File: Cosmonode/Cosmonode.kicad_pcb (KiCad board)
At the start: 2 copper layers, 47 x 34.3 mm, 36 parts, among them J1 CONN_01X08, J10 WEEE_Logo, J11 Aloes_Logo, J12 Aloes_mini_Logo, J2 CONN_01X08, J3 CONN_01X09, J4 OSHW, J5 CONN_01X02, J6 GS3, J7 Kicad_Logo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

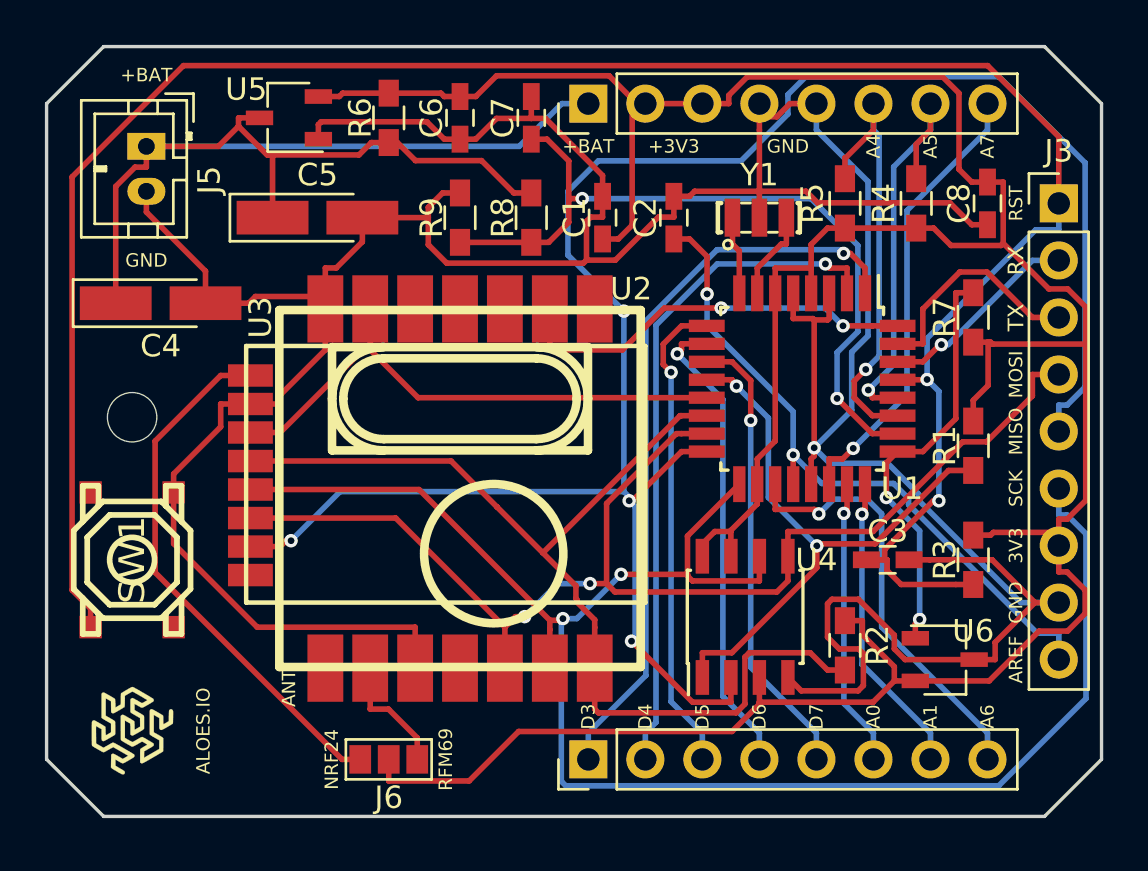
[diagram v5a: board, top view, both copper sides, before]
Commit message: update to v0.5 ( base, ext05, ext07, ext08 )
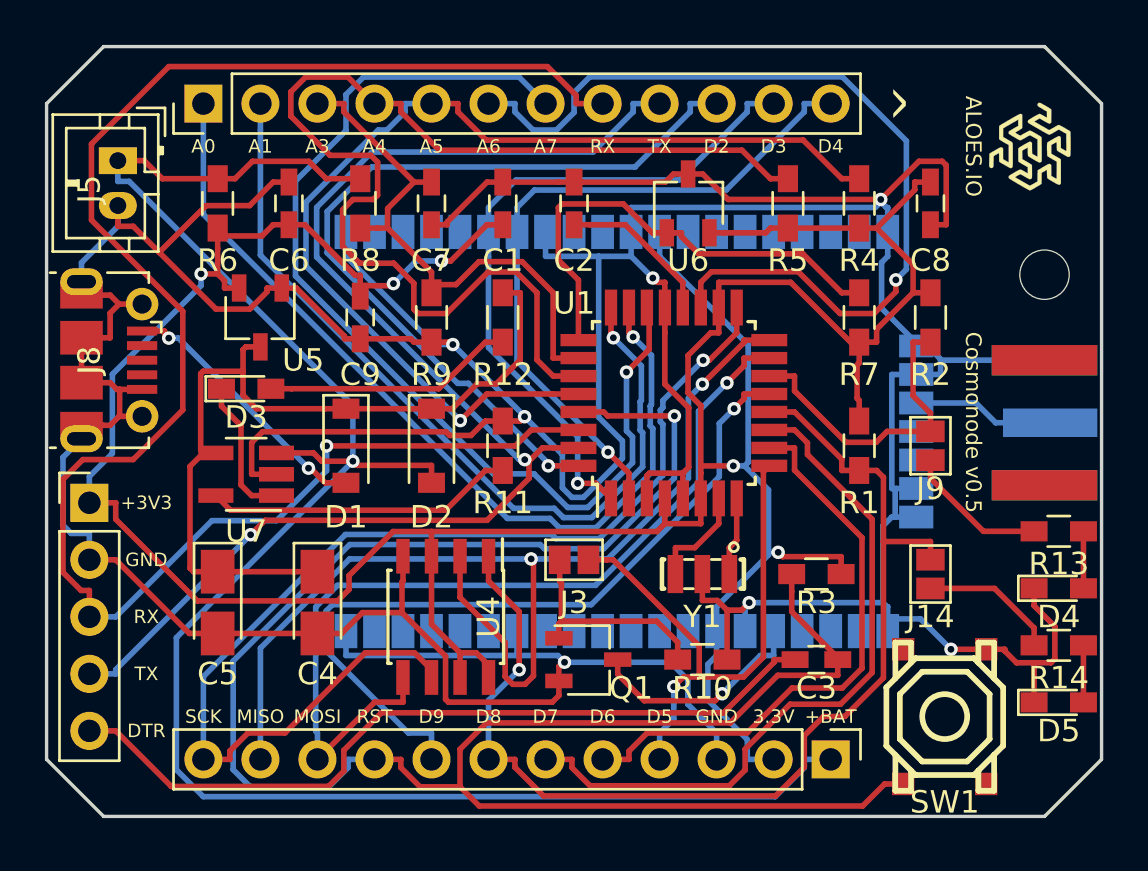
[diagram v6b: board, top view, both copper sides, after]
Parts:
- removed J6: GS3, Connectors:GS3
- removed J7: Kicad_Logo, Symbols:KiCad-Logo2_6mm_SilkScreen
- removed U2: RFM69CW, w_rf_modules:RFM12B_SMD
- added C9: 100nF, Capacitors_SMD:C_0603_HandSoldering, F.Cu at (160.0, 89.5)
- added D1: MBR0520, Diodes_SMD:D_SOD-123, F.Cu at (159.4, 95.2)
- added D2: MBR0520, Diodes_SMD:D_SOD-123, F.Cu at (163.2, 95.2)
- added D3: LED, LEDs:LED_0603_HandSoldering, F.Cu at (154.9, 92.7)
- added D4: LED, LEDs:LED_0603_HandSoldering, F.Cu at (191.1, 101.6)
- added D5: LED, LEDs:LED_0603_HandSoldering, F.Cu at (191.1, 106.7)
- added J13: CONN_01X05, Pin_Headers:Pin_Header_Straight_1x05_Pitch2.54mm, F.Cu at (148.0, 97.8)
- added J14: GS2, Connectors:GS2, F.Cu at (185.4, 101.0)
- added J8: USB_OTG, Connectors_USB:USB_Micro-B_Molex-105017-0001, F.Cu at (148.0, 91.4)
- added J9: GS2, Connectors:GS2, F.Cu at (185.4, 95.2)
- added P1: COAX, sma:EDGE_SMA_5, B.Cu at (190.5, 91.4)
- added Q1: BSS123, TO_SOT_Packages_SMD:TSOT-23, F.Cu at (170.2, 104.8)
- added R10: 10k, Resistors_SMD:R_0603_HandSoldering, F.Cu at (175.3, 104.8)
- added R11: R, Resistors_SMD:R_0603_HandSoldering, F.Cu at (166.4, 95.2)
- added R12: 1k, Resistors_SMD:R_0603_HandSoldering, F.Cu at (166.4, 89.5)
- added R13: 1k, Resistors_SMD:R_0603_HandSoldering, F.Cu at (191.1, 99.1)
- added R14: 1k, Resistors_SMD:R_0603_HandSoldering, F.Cu at (191.1, 104.1)
- added U7: MCP73811T-420I/OT, TO_SOT_Packages_SMD:SOT-23-5_HandSoldering, F.Cu at (154.9, 96.5)
- C4, C5: footprint Capacitors_Tantalum_SMD:CP_Tantalum_Case-A_EIA-3216-18_Hand -> Capacitors_Tantalum_SMD:CP_Tantalum_Case-A_EIA-3216-18_Reflow
- J1, J2: value CONN_01X08 -> CONN_01X12; footprint Pin_Headers:Pin_Header_Straight_1x08_Pitch2.54mm -> Pin_Headers:Pin_Header_Straight_1x12_Pitch2.54mm
- J3: value CONN_01X09 -> GS2; footprint Pin_Headers:Pin_Header_Straight_1x09_Pitch2.54mm -> Connectors:GS2
- U3: value NRF24L01_Breakout -> RN2483; footprint mysensors_radios:NRF24L01-SMD -> RN2483:RN2483; moved to B.Cu
- moved J12 47.7 mm to (189.9, 81.9), turned to 270 degrees
- moved MK1 41.1 mm to (190.5, 87.6)
- moved SW1 36.9 mm to (186.1, 107.3)
- moved J11 35.8 mm to (187.3, 82.5), turned to 90 degrees
- moved J1 33.9 mm to (153.0, 80.0)
- moved J2 31.1 mm to (181.0, 109.2), turned to 270 degrees
- moved J3 26.8 mm to (169.5, 100.3), turned to 90 degrees
- moved U6 23.3 mm to (174.6, 84.5), turned to 90 degrees
- moved C5 17.7 mm to (153.7, 102.2), turned to 270 degrees
- moved Y1 16.1 mm to (175.3, 101.0), turned to 180 degrees
- moved R2 15.1 mm to (185.4, 89.5)
- moved C4 15.1 mm to (158.1, 102.2), turned to 270 degrees
- moved U4 13.3 mm to (163.8, 102.9), turned to 270 degrees
- moved J4 12.8 mm to (188.6, 102.2), turned to 90 degrees
- moved U3 9.03 mm to (158.1, 103.5), turned to 90 degrees
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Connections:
- net /A2 renamed A2
- C3 pad 1: /RST -> RST
- C3 pad 2: GND -> DTR
- C4 pad 1: /BAT+ -> Net-(C4-Pad1)
- C5 pad 1: /BAT+ -> Net-(C4-Pad1)
- C7 pad 2: /A3 -> A3
- J1 pad 1: /D3 -> A0
- J1 pad 2: /D4 -> A1
- J1 pad 3: /D5 -> A3
- J1 pad 4: /D6 -> A4
- J1 pad 5: /D7 -> A5
- J1 pad 6: /A0 -> A6
- J1 pad 7: /A1 -> A7
- J1 pad 8: /A6 -> RX
- J2 pad 1: /BAT+ -> +BATT
- J2 pad 3: +3V3 -> GND
- J2 pad 4: GND -> D5
- J2 pad 5: GND -> D6
- J2 pad 6: /A4 -> D7
- J2 pad 7: /A5 -> D8
- J2 pad 8: /A7 -> D9
- J3 pad 1: /RST -> Net-(J3-Pad1)
- J3 pad 2: /RX -> D5
- J5 pad 1: /BAT+ -> +BATT
- R1 pad 2: /D8 -> D8
- R2 pad 2: /D10 -> D10
- R3 pad 2: /RST -> RST
- R4 pad 2: /A5 -> A5
- R5 pad 2: /A4 -> A4
- R6 pad 2: /BAT+ -> +BATT
- R8 pad 1: /BAT+ -> +BATT
- R8 pad 2: /A3 -> A3
- R9 pad 1: /A3 -> A3
- SW1 pad 2: /RST -> RST
- U1 pad 1: /D3 -> D3
- U1 pad 10: /D6 -> D6
- U1 pad 11: /D7 -> D7
- U1 pad 12: /D8 -> D8
- U1 pad 13: /D9 -> D9
- U1 pad 14: /D10 -> D10
- U1 pad 15: /MOSI -> MOSI
- U1 pad 16: /MISO -> MISO
- U1 pad 17: /SCK -> SCK
- U1 pad 19: /A6 -> A6
- U1 pad 2: /D4 -> D4
- U1 pad 22: /A7 -> A7
- U1 pad 23: /A0 -> A0
- U1 pad 24: /A1 -> A1
- U1 pad 26: /A3 -> A3
- U1 pad 27: /A4 -> A4
- U1 pad 28: /A5 -> A5
- U1 pad 29: /RST -> RST
- U1 pad 30: /RX -> RX
- U1 pad 31: /TX -> TX
- U1 pad 32: /D2 -> D2
- U1 pad 9: /D5 -> D5
- U3 pad 2: /VCC_NRF24 -> Net-(U3-Pad2)
- U3 pad 3: /D9 -> Net-(U3-Pad3)
- U3 pad 4: /D10 -> Net-(U3-Pad4)
- U3 pad 5: /SCK -> Net-(U3-Pad5)
- U3 pad 6: /MOSI -> D3
- U3 pad 7: /MISO -> D4
- U3 pad 8: Net-(U3-Pad8) -> GND
- U4 pad 1: /D8 -> D8
- U4 pad 2: /MISO -> MISO
- U4 pad 5: /MOSI -> MOSI
- U4 pad 6: /SCK -> SCK
- U5 pad 3: /BAT+ -> Net-(C4-Pad1)
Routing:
- net /RST: track 97.8 -> 0.00 mm, vias 2 -> 0
- net RST: track 0.00 -> 92.7 mm, vias 0 -> 1
- net /MISO: track 91.3 -> 0.00 mm, vias 4 -> 0
- net GND: track 178.6 -> 268.2 mm, vias 1 -> 7
- net +BATT: track 0.00 -> 85.2 mm, vias 0 -> 1
- net RX: track 0.00 -> 77.9 mm, vias 0 -> 1
- net /SCK: track 76.7 -> 0.00 mm, vias 2 -> 0
- net TX: track 0.00 -> 59.4 mm, vias 0 -> 2
- net /MOSI: track 56.0 -> 0.00 mm, vias 2 -> 0
- net A4: track 0.00 -> 52.1 mm
- net /BAT+: track 51.6 -> 0.00 mm
- net SCK: track 0.00 -> 50.1 mm, vias 0 -> 1
- net D8: track 0.00 -> 50.1 mm, vias 0 -> 1
- net MISO: track 0.00 -> 48.5 mm, vias 0 -> 2
- net A5: track 0.00 -> 46.6 mm, vias 0 -> 1
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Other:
- board text added: "3.3V"
- board text added: "A3"
- board text added: "Cosmonode v0.5"
- board text added: "Cosmonode v0.5, by Getlarge https://aloes.io"
- board text added: "D2"
- board text added: "D8"
- board text added: "D9"
- board text added: "DTR"
- board text added: "^"
- board text removed: "3V3"
- board text removed: "ALOES"
- board text removed: "ANT"
- board text removed: "AREF"
- board text removed: "Cosmonode v0.3, by Getlarge https://aloes.io https://framagit.org/aloes"
- board text removed: "Do it yourself and do your best"
- board text removed: "NRF24"
- board text removed: "RFM69"

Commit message: update to V0.7 (WIP)
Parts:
- removed Q1: BSS123, TO_SOT_Packages_SMD:TSOT-23
- removed R10, R2: 10k, Resistors_SMD:R_0603_HandSoldering
- removed U4: M25P40, Housings_SOIC:SOIC-8_3.9x4.9mm_Pitch1.27mm
- added J6: GS2, Connectors:GS2, F.Cu at (165.7, 100.3)
- added JP1: Jumper_NO_Small, Pin_Headers:Pin_Header_Straight_1x02_Pitch2.54mm, F.Cu at (147.3, 105.4)
- added U2: RFM69CW, w_rf_modules:RFM12B_SMD, B.Cu at (174.0, 94.6)
- moved J10 39.3 mm to (154.9, 88.3)
- moved D4 17.1 mm to (186.7, 85.1), turned to 270 degrees
- moved D3 14.5 mm to (149.2, 79.4)
- moved C8 12.1 mm to (184.8, 96.5)
- moved J9 11.0 mm to (183.5, 84.5)
- moved C3 10.9 mm to (169.5, 103.5), turned to 270 degrees
- moved R14 10.8 mm to (180.3, 103.5), turned to 90 degrees
- moved R13 10.4 mm to (184.8, 90.8), turned to 270 degrees
- moved MK1 7.10 mm to (189.2, 80.6)
- moved C5 7.01 mm to (160.7, 102.9), turned to 90 degrees
- moved D5 6.75 mm to (186.7, 101.6), turned to 270 degrees
- moved J3 5.39 mm to (165.7, 104.1), turned to 270 degrees
- moved R3 4.07 mm to (177.2, 103.5), turned to 90 degrees
- moved J11 3.86 mm to (188.0, 86.4)
- moved Y1 3.17 mm to (173.4, 103.5), turned to 90 degrees
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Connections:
- net Net-(P1-Pad1) renamed ANT
- net SCK renamed D13/SCK
- D1 pad 1: Net-(C4-Pad1) -> Net-(D1-Pad1)
- D2 pad 1: Net-(C4-Pad1) -> Net-(D1-Pad1)
- J14 pad 2: D8 -> A7
- J2 pad 10: MOSI -> D11/MOSI
- J2 pad 11: MISO -> D12/MISO
- J3 pad 1: Net-(J3-Pad1) -> /RADIO_RESET
- J3 pad 2: D5 -> D12/MISO
- J9 pad 2: D10 -> A6
- P1 pad 3: GND -> (no net)
- P1 pad 4: GND -> (no net)
- P1 pad 5: GND -> (no net)
- R12 pad 2: Net-(C4-Pad1) -> Net-(D1-Pad1)
- U1 pad 15: MOSI -> D11/MOSI
- U1 pad 16: MISO -> D12/MISO
- U3 pad 6: D3 -> D11/MOSI
- U3 pad 7: D4 -> D10
- U7 pad 4: Net-(C4-Pad1) -> Net-(D1-Pad1)
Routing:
- net GND: track 268.2 -> 0.00 mm, vias 7 -> 0
- net +3V3: track 150.2 -> 0.00 mm, vias 5 -> 0
- net RST: track 92.7 -> 0.00 mm, vias 1 -> 0
- net +BATT: track 85.2 -> 0.00 mm, vias 1 -> 0
- net RX: track 77.9 -> 0.00 mm, vias 1 -> 0
- net TX: track 59.4 -> 0.00 mm, vias 2 -> 0
- net A4: track 52.1 -> 0.00 mm
- net D13/SCK: track 50.1 -> 0.00 mm, vias 1 -> 0
- net D8: track 50.1 -> 0.00 mm, vias 1 -> 0
- net MISO: track 48.5 -> 0.00 mm, vias 2 -> 0
- net A5: track 46.6 -> 0.00 mm, vias 1 -> 0
- net A7: track 46.3 -> 0.00 mm, vias 1 -> 0
- net A6: track 40.1 -> 0.00 mm, vias 1 -> 0
- net MOSI: track 39.6 -> 0.00 mm, vias 1 -> 0
- net A0: track 39.5 -> 0.00 mm, vias 1 -> 0
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- removed copper zone on B.Cu, net GND
- removed copper zone on F.Cu, net GND
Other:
- board text added: "Cosmonode v0.7"
- board text added: "[ ]RFM69CW"
- board text added: "[ ]RN2483"
- board text removed: "Cosmonode v0.5"
- board text removed: "Cosmonode v0.5, by Getlarge https://aloes.io"

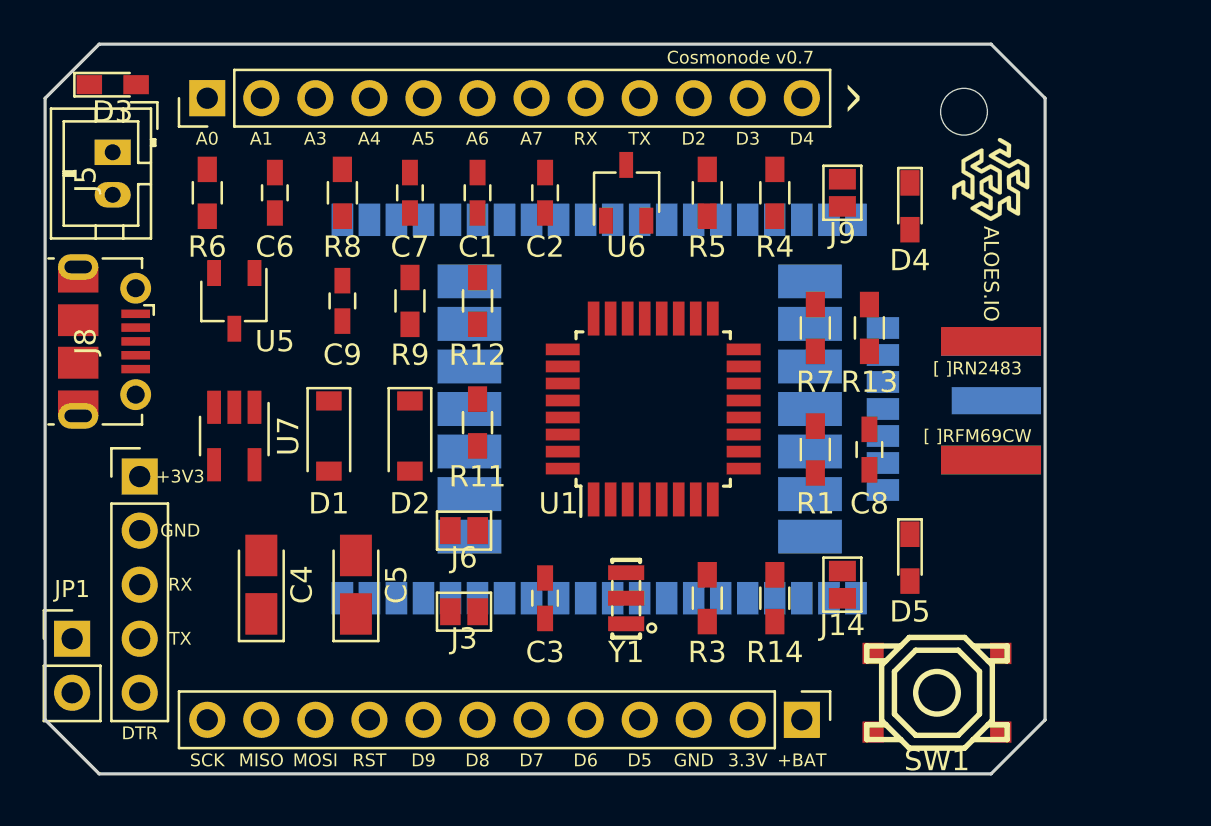
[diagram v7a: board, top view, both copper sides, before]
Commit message: near v0.7 ( mother and ext02 ), add mini extension
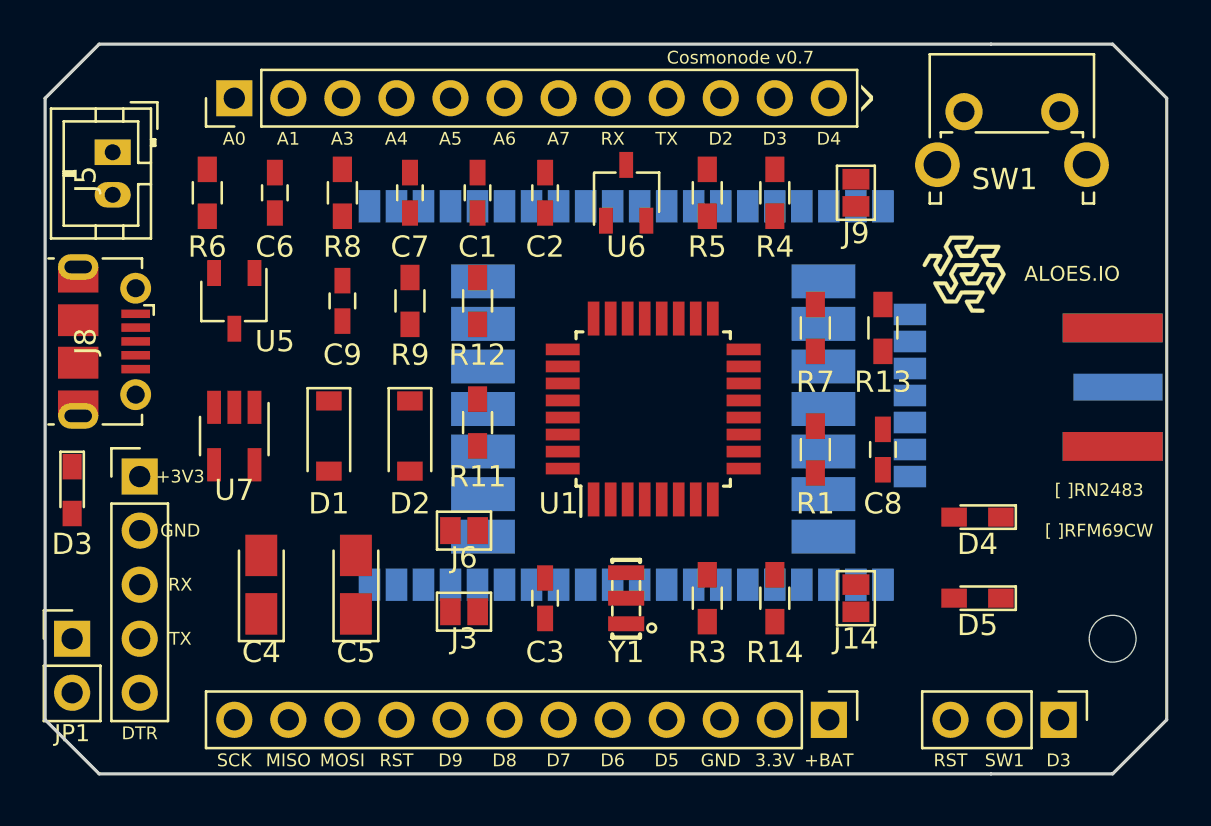
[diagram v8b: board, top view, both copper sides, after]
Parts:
- added JP2: Jumper_NC_Dual, Pin_Headers:Pin_Header_Straight_1x03_Pitch2.54mm, F.Cu at (193.7, 109.2)
- SW1: footprint w_switch:smd_push2 -> Buttons_Switches_THT:SW_Tactile_SPST_Angled_PTS645Vx58-2LFS
- moved J4 32.0 mm to (157.5, 95.2)
- moved J11 30.5 mm to (157.5, 86.4)
- moved SW1 27.3 mm to (189.2, 80.6), turned to 0 degrees
- moved MK1 25.7 mm to (196.2, 105.4)
- moved D3 19.1 mm to (147.3, 98.4), turned to 270 degrees
- moved D4 14.9 mm to (189.9, 99.7), turned to 180 degrees
- moved J10 14.1 mm to (156.8, 102.2)
- moved P1 5.75 mm to (196.2, 90.8)
- moved J12 4.62 mm to (189.2, 88.3), turned to 0 degrees
- moved D5 3.70 mm to (189.9, 103.5), turned to 180 degrees
- moved U3 1.42 mm to (160.0, 102.9)
- moved J1 1.27 mm to (154.9, 80.0)
- moved J2 1.27 mm to (182.9, 109.2)
- moved J14 0.90 mm to (184.2, 103.5)
- moved J9 0.64 mm to (184.2, 84.5)
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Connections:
- J3 pad 2: D12/MISO -> D9
- J6 pad 1: D3 -> D2
- SW1 pad 2: RST -> Net-(JP2-Pad2)
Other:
- board size 47 x 34.3 mm -> 52.7 x 34.3 mm
- board text added: "SW1"
